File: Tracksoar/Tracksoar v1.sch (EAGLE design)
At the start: 39 parts, among them IC2 74AHC1G125DBV, U1 ATMEGA328P, Y1 16MHZ

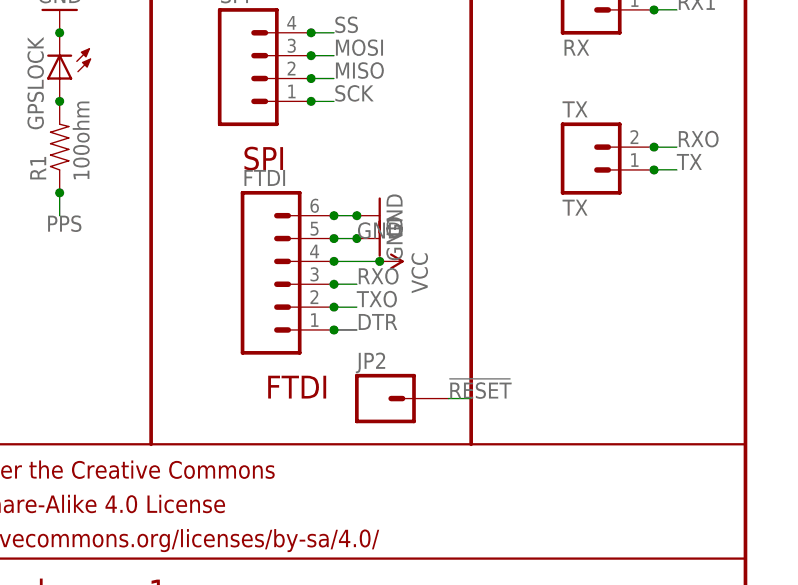
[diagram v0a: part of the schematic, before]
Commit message: replace headers
replaced 2.54mm headers on all production boards with 2mm headers to
resolve daughter board issues.
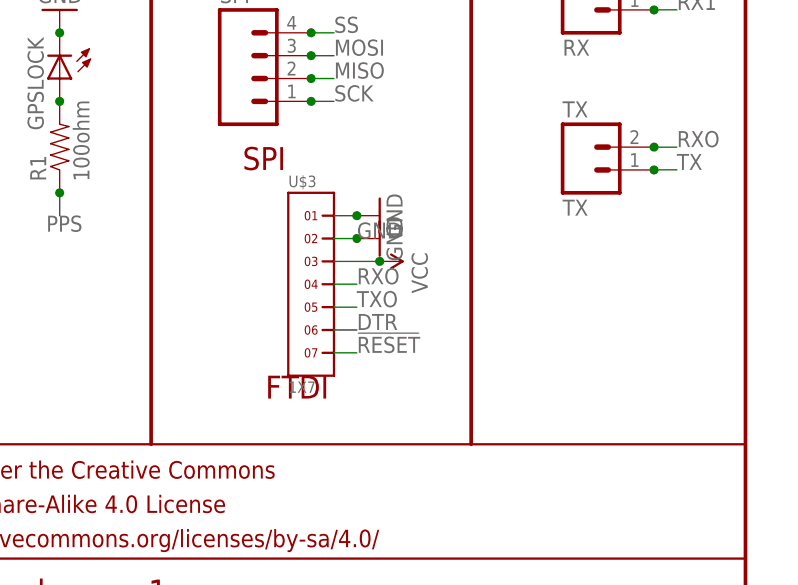
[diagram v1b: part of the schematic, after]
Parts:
- removed FTDI: (no value), SparkFun-Connectors:M06NO_SILK_FEMALE_PTH
- removed JP2: (no value), SparkFun-Connectors:M01PTH
- added U$3: 1X7, headers(2mm):1X7
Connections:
- net !RESET: now also U$3.7; no longer JP2.1
- net DTR: now also U$3.6; no longer FTDI.1
- net GND: now also U$3.1, U$3.2; no longer FTDI.5, FTDI.6
- net RXO: now also U$3.4; no longer FTDI.3
- net TXO: now also U$3.5; no longer FTDI.2
- net VCC: now also U$3.3; no longer FTDI.4
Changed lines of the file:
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@@
 <part name="SUPPLY4" library="SparkFun-Aesthetics" deviceset="VCC" device=""/>
 <part name="SUPPLY5" library="SparkFun-Aesthetics" deviceset="VCC" device=""/>
-<part name="FTDI" library="SparkFun-Connectors" deviceset="M06" device="NO_SILK_FEMALE_PTH"/>
 <part name="SUPPLY7" library="SparkFun-Aesthetics" deviceset="VCC" device=""/>
 <part name="SUPPLY8" library="SparkFun-Aesthetics" deviceset="VCC" device=""/>
@@
 <part name="GPS-ANT" library="SparkFun-RF" deviceset="ANTENNA2" device="SMD3"/>
 <part name="TX1" library="SparkFun-Connectors" deviceset="M02" device="JST-PTH-VERT" value="TX"/>
-<part name="JP2" library="SparkFun-Connectors" deviceset="M01" device="PTH"/>
+<part name="U$3" library="headers(2mm)" deviceset="1X7" device=""/>
 </parts>
 <sheets>
@@
 <instance part="SUPPLY4" gate="G$1" x="55.88" y="160.02" rot="R90"/>
 <instance part="SUPPLY5" gate="G$1" x="55.88" y="152.4" rot="R90"/>
-<instance part="FTDI" gate="G$1" x="198.12" y="53.34"/>
 <instance part="SUPPLY7" gate="G$1" x="25.4" y="60.96" rot="R90"/>
 <instance part="SUPPLY8" gate="G$1" x="25.4" y="58.42" rot="R90"/>
@@
 <instance part="GPS-ANT" gate="G$1" x="165.1" y="165.1" rot="R90"/>
 <instance part="TX1" gate="G$1" x="193.04" y="91.44"/>
-<instance part="JP2" gate="G$1" x="208.28" y="40.64"/>
+<instance part="U$3" gate="G$1" x="200.66" y="53.34"/>
 </instances>
 <busses>
@@
 </segment>
 <segment>
-<pinref part="FTDI" gate="G$1" pin="6"/>
 <wire x1="203.2" y1="60.96" x2="205.74" y2="60.96" width="0.1524" layer="91"/>
 <pinref part="GND22" gate="1" pin="GND"/>
-<junction x="203.2" y="60.96"/>
 <junction x="205.74" y="60.96"/>
+<pinref part="U$3" gate="G$1" pin="1"/>
 </segment>
 <segment>
@@
 </segment>
 <segment>
-<pinref part="FTDI" gate="G$1" pin="5"/>
 <wire x1="203.2" y1="58.42" x2="205.74" y2="58.42" width="0.1524" layer="91"/>
 <label x="205.74" y="58.42" size="1.778" layer="95"/>
-<junction x="203.2" y="58.42"/>
 <pinref part="GND10" gate="1" pin="GND"/>
 <junction x="205.74" y="58.42"/>
+<pinref part="U$3" gate="G$1" pin="2"/>
 </segment>
 <segment>
@@
 </segment>
 <segment>
-<pinref part="FTDI" gate="G$1" pin="4"/>
 <wire x1="203.2" y1="55.88" x2="208.28" y2="55.88" width="0.1524" layer="91"/>
 <pinref part="SUPPLY9" gate="G$1" pin="VCC"/>
-<junction x="203.2" y="55.88"/>
 <junction x="208.28" y="55.88"/>
+<pinref part="U$3" gate="G$1" pin="3"/>
 </segment>
 <segment>
@@
 <net name="DTR" class="0">
 <segment>
-<pinref part="FTDI" gate="G$1" pin="1"/>
 <wire x1="203.2" y1="48.26" x2="205.74" y2="48.26" width="0.1524" layer="91"/>
 <label x="205.74" y="48.26" size="1.778" layer="95"/>
-<junction x="203.2" y="48.26"/>
+<pinref part="U$3" gate="G$1" pin="6"/>
 </segment>
 <segment>
@@
 </segment>
 <segment>
-<pinref part="FTDI" gate="G$1" pin="3"/>
 <wire x1="203.2" y1="53.34" x2="205.74" y2="53.34" width="0.1524" layer="91"/>
 <label x="205.74" y="53.34" size="1.778" layer="95"/>
-<junction x="203.2" y="53.34"/>
+<pinref part="U$3" gate="G$1" pin="4"/>
 </segment>
 </net>
@@
 </segment>
 <segment>
-<pinref part="FTDI" gate="G$1" pin="2"/>
 <wire x1="203.2" y1="50.8" x2="205.74" y2="50.8" width="0.1524" layer="91"/>
 <label x="205.74" y="50.8" size="1.778" layer="95"/>
-<junction x="203.2" y="50.8"/>
+<pinref part="U$3" gate="G$1" pin="5"/>
 </segment>
 </net>
@@
 <net name="!RESET" class="0">
 <segment>
-<pinref part="JP2" gate="G$1" pin="1"/>
-<wire x1="215.9" y1="40.64" x2="218.44" y2="40.64" width="0.1524" layer="91"/>
-<label x="215.9" y="40.64" size="1.778" layer="95"/>
-</segment>
-<segment>
+<wire x1="203.2" y1="45.72" x2="205.74" y2="45.72" width="0.1524" layer="91"/>
+<label x="205.74" y="45.72" size="1.778" layer="95"/>
+<pinref part="U$3" gate="G$1" pin="7"/>
+</segment>
+<segment>

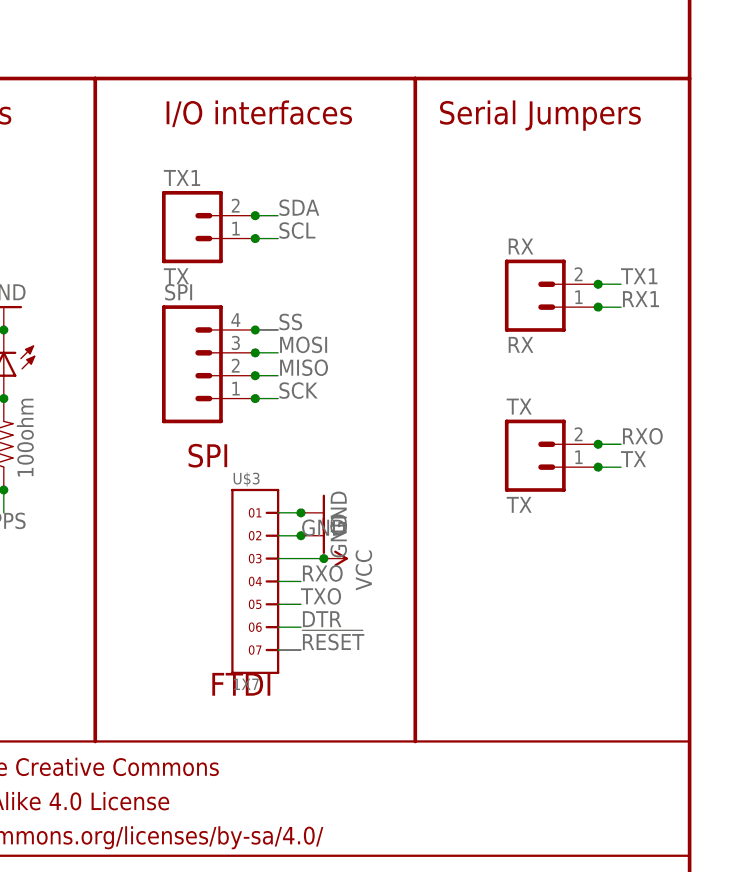
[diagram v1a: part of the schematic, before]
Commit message: Rounded corners
Added rounded corners to the tracksoar v1
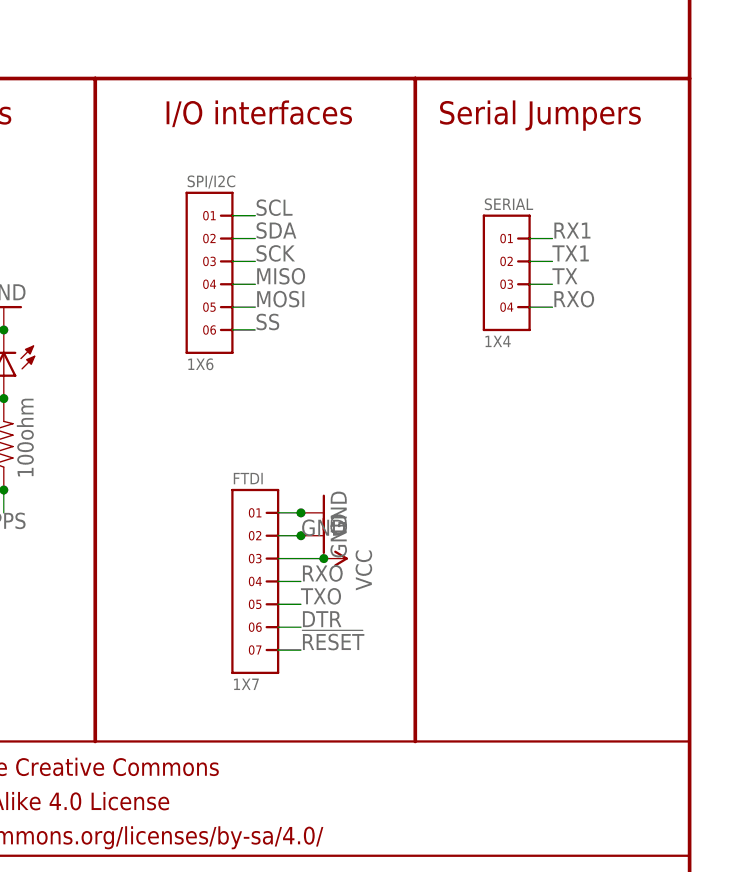
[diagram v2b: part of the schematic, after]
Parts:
- removed RX: RX, SparkFun-Connectors:M02JST-PTH-VERT
- removed SPI: (no value), SparkFun-Connectors:M04JST-PTH-VERT
- removed TX, TX1: TX, SparkFun-Connectors:M02JST-PTH-VERT
- added SERIAL: 1X4, headers(2mm):1X4
- added SPI/I2C: 1X6, headers(2mm):1X6
- renumbered U$3 to FTDI
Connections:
- net MISO: now also SPI/I2C.4; no longer SPI.2
- net MOSI: now also SPI/I2C.5; no longer SPI.3
- net RX1: now also SERIAL.1; no longer RX.1
- net RXO: now also SERIAL.4; no longer TX.2
- net SCK: now also SPI/I2C.3; no longer SPI.1
- net SCL: now also SPI/I2C.1; no longer TX1.1
- net SDA: now also SPI/I2C.2; no longer TX1.2
- net SS: now also SPI/I2C.6; no longer SPI.4
- net TX: now also SERIAL.3; no longer TX.1
- net TX1: now also SERIAL.2; no longer RX.2
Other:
- note removed: "FTDI"
- note removed: "SPI"
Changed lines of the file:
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@@
 <part name="SUPPLY10" library="SparkFun-Aesthetics" deviceset="VCC" device=""/>
 <part name="C5" library="SparkFun-Capacitors" deviceset="CAP" device="0805" value=".1uf"/>
-<part name="TX" library="SparkFun-Connectors" deviceset="M02" device="JST-PTH-VERT" value="TX"/>
-<part name="SPI" library="SparkFun-Connectors" deviceset="M04" device="JST-PTH-VERT"/>
 <part name="FRAME1" library="SparkFun-Aesthetics" deviceset="FRAME-LETTER" device=""/>
 <part name="SUPPLY11" library="SparkFun-Aesthetics" deviceset="VCC" device=""/>
@@
 <part name="GND1" library="SparkFun-Aesthetics" deviceset="GND" device=""/>
 <part name="GND3" library="SparkFun-Aesthetics" deviceset="GND" device=""/>
-<part name="RX" library="SparkFun-Connectors" deviceset="M02" device="JST-PTH-VERT" value="RX"/>
 <part name="GND10" library="SparkFun-Aesthetics" deviceset="GND" device=""/>
 <part name="BMP180" library="SparkFun-Sensors" deviceset="BMP180" device=""/>
@@
 <part name="SHT21" library="sht21" deviceset="SHT21" device=""/>
 <part name="GPS-ANT" library="SparkFun-RF" deviceset="ANTENNA2" device="SMD3"/>
-<part name="TX1" library="SparkFun-Connectors" deviceset="M02" device="JST-PTH-VERT" value="TX"/>
-<part name="U$3" library="headers(2mm)" deviceset="1X7" device=""/>
+<part name="FTDI" library="headers(2mm)" deviceset="1X7" device=""/>
+<part name="SPI/I2C" library="headers(2mm)" deviceset="1X6" device=""/>
+<part name="SERIAL" library="headers(2mm)" deviceset="1X4" device=""/>
 </parts>
 <sheets>
@@
 <text x="190.5" y="104.14" size="2.54" layer="94">I/O interfaces</text>
 <text x="220.98" y="104.14" size="2.54" layer="94">Serial Jumpers</text>
-<text x="193.04" y="66.04" size="2.54" layer="94">SPI</text>
-<text x="195.58" y="40.64" size="2.54" layer="94">FTDI</text>
 <wire x1="147.32" y1="35.56" x2="83.82" y2="35.56" width="0.1524" layer="94"/>
 <text x="111.76" y="104.14" size="1.778" layer="94">Sensors</text>
@@
 <instance part="SUPPLY10" gate="G$1" x="25.4" y="78.74"/>
 <instance part="C5" gate="G$1" x="12.7" y="68.58" rot="R90"/>
-<instance part="TX" gate="G$1" x="231.14" y="66.04"/>
-<instance part="SPI" gate="G$1" x="195.58" y="76.2"/>
 <instance part="FRAME1" gate="G$1" x="0" y="0"/>
 <instance part="FRAME1" gate="G$2" x="147.32" y="0"/>
@@
 <instance part="GND1" gate="1" x="66.04" y="167.64" rot="R90"/>
 <instance part="GND3" gate="1" x="17.78" y="157.48"/>
-<instance part="RX" gate="G$1" x="231.14" y="83.82"/>
 <instance part="GND10" gate="1" x="208.28" y="58.42" rot="R90"/>
 <instance part="BMP180" gate="G$1" x="104.14" y="48.26"/>
@@
 <instance part="SHT21" gate="A" x="121.92" y="83.82"/>
 <instance part="GPS-ANT" gate="G$1" x="165.1" y="165.1" rot="R90"/>
-<instance part="TX1" gate="G$1" x="193.04" y="91.44"/>
-<instance part="U$3" gate="G$1" x="200.66" y="53.34"/>
+<instance part="FTDI" gate="G$1" x="200.66" y="53.34"/>
+<instance part="SPI/I2C" gate="G$1" x="195.58" y="86.36"/>
+<instance part="SERIAL" gate="G$1" x="228.6" y="86.36"/>
 </instances>
 <busses>
@@
 <pinref part="GND22" gate="1" pin="GND"/>
 <junction x="205.74" y="60.96"/>
-<pinref part="U$3" gate="G$1" pin="1"/>
+<pinref part="FTDI" gate="G$1" pin="1"/>
 </segment>
 <segment>
@@
 <pinref part="GND10" gate="1" pin="GND"/>
 <junction x="205.74" y="58.42"/>
-<pinref part="U$3" gate="G$1" pin="2"/>
+<pinref part="FTDI" gate="G$1" pin="2"/>
 </segment>
 <segment>
@@
 <pinref part="SUPPLY9" gate="G$1" pin="VCC"/>
 <junction x="208.28" y="55.88"/>
-<pinref part="U$3" gate="G$1" pin="3"/>
+<pinref part="FTDI" gate="G$1" pin="3"/>
 </segment>
 <segment>
@@
 <wire x1="203.2" y1="48.26" x2="205.74" y2="48.26" width="0.1524" layer="91"/>
 <label x="205.74" y="48.26" size="1.778" layer="95"/>
-<pinref part="U$3" gate="G$1" pin="6"/>
+<pinref part="FTDI" gate="G$1" pin="6"/>
 </segment>
 <segment>
@@
 </segment>
 <segment>
-<pinref part="TX" gate="G$1" pin="2"/>
-<wire x1="238.76" y1="68.58" x2="241.3" y2="68.58" width="0.1524" layer="91"/>
-<label x="241.3" y="68.58" size="1.778" layer="95"/>
-<junction x="238.76" y="68.58"/>
+<wire x1="233.68" y1="83.82" x2="231.14" y2="83.82" width="0.1524" layer="91"/>
+<label x="233.68" y="83.82" size="1.778" layer="95"/>
+<pinref part="SERIAL" gate="G$1" pin="4"/>
 </segment>
 <segment>
 <wire x1="203.2" y1="53.34" x2="205.74" y2="53.34" width="0.1524" layer="91"/>
 <label x="205.74" y="53.34" size="1.778" layer="95"/>
-<pinref part="U$3" gate="G$1" pin="4"/>
+<pinref part="FTDI" gate="G$1" pin="4"/>
 </segment>
 </net>
@@
 <wire x1="203.2" y1="50.8" x2="205.74" y2="50.8" width="0.1524" layer="91"/>
 <label x="205.74" y="50.8" size="1.778" layer="95"/>
-<pinref part="U$3" gate="G$1" pin="5"/>
+<pinref part="FTDI" gate="G$1" pin="5"/>
 </segment>
 </net>
@@
 </segment>
 <segment>
-<pinref part="SPI" gate="G$1" pin="2"/>
-<wire x1="200.66" y1="76.2" x2="203.2" y2="76.2" width="0.1524" layer="91"/>
-<label x="203.2" y="76.2" size="1.778" layer="95"/>
-<junction x="200.66" y="76.2"/>
+<wire x1="200.66" y1="86.36" x2="198.12" y2="86.36" width="0.1524" layer="91"/>
+<label x="200.66" y="86.36" size="1.778" layer="95"/>
+<pinref part="SPI/I2C" gate="G$1" pin="4"/>
 </segment>
 </net>
@@
 </segment>
 <segment>
-<pinref part="SPI" gate="G$1" pin="3"/>
-<wire x1="200.66" y1="78.74" x2="203.2" y2="78.74" width="0.1524" layer="91"/>
-<label x="203.2" y="78.74" size="1.778" layer="95"/>
-<junction x="200.66" y="78.74"/>
+<wire x1="200.66" y1="83.82" x2="198.12" y2="83.82" width="0.1524" layer="91"/>
+<label x="200.66" y="83.82" size="1.778" layer="95"/>
+<pinref part="SPI/I2C" gate="G$1" pin="5"/>
 </segment>
 </net>
@@
 </segment>
 <segment>
-<pinref part="SPI" gate="G$1" pin="1"/>
-<wire x1="200.66" y1="73.66" x2="203.2" y2="73.66" width="0.1524" layer="91"/>
-<label x="203.2" y="73.66" size="1.778" layer="95"/>
-<junction x="200.66" y="73.66"/>
+<wire x1="200.66" y1="88.9" x2="198.12" y2="88.9" width="0.1524" layer="91"/>
+<label x="200.66" y="88.9" size="1.778" layer="95"/>
+<pinref part="SPI/I2C" gate="G$1" pin="3"/>
 </segment>
 </net>
@@
 </segment>
 <segment>
-<pinref part="SPI" gate="G$1" pin="4"/>
-<wire x1="200.66" y1="81.28" x2="203.2" y2="81.28" width="0.1524" layer="91"/>
-<label x="203.2" y="81.28" size="1.778" layer="95"/>
-<junction x="200.66" y="81.28"/>
+<wire x1="200.66" y1="81.28" x2="198.12" y2="81.28" width="0.1524" layer="91"/>
+<label x="200.66" y="81.28" size="1.778" layer="95"/>
+<pinref part="SPI/I2C" gate="G$1" pin="6"/>
 </segment>
 </net>
@@
 </segment>
 <segment>
-<pinref part="RX" gate="G$1" pin="2"/>
-<wire x1="238.76" y1="86.36" x2="241.3" y2="86.36" width="0.1524" layer="91"/>
-<label x="241.3" y="86.36" size="1.778" layer="95"/>
-<junction x="238.76" y="86.36"/>
+<label x="233.68" y="88.9" size="1.778" layer="95"/>
+<pinref part="SERIAL" gate="G$1" pin="2"/>
+<wire x1="231.14" y1="88.9" x2="233.68" y2="88.9" width="0.1524" layer="91"/>
 </segment>
 </net>
@@
 </segment>
 <segment>
-<pinref part="TX1" gate="G$1" pin="2"/>
-<wire x1="200.66" y1="93.98" x2="203.2" y2="93.98" width="0.1524" layer="91"/>
-<label x="203.2" y="93.98" size="1.778" layer="95"/>
-<junction x="200.66" y="93.98"/>
+<wire x1="200.66" y1="91.44" x2="198.12" y2="91.44" width="0.1524" layer="91"/>
+<label x="200.66" y="91.44" size="1.778" layer="95"/>
+<pinref part="SPI/I2C" gate="G$1" pin="2"/>
 </segment>
 </net>
@@
 </segment>
 <segment>
-<pinref part="TX1" gate="G$1" pin="1"/>
-<wire x1="200.66" y1="91.44" x2="203.2" y2="91.44" width="0.1524" layer="91"/>
-<label x="203.2" y="91.44" size="1.778" layer="95"/>
-<junction x="200.66" y="91.44"/>
+<wire x1="200.66" y1="93.98" x2="198.12" y2="93.98" width="0.1524" layer="91"/>
+<label x="200.66" y="93.98" size="1.778" layer="95"/>
+<pinref part="SPI/I2C" gate="G$1" pin="1"/>
 </segment>
 </net>
@@
 </segment>
 <segment>
-<pinref part="RX" gate="G$1" pin="1"/>
-<wire x1="238.76" y1="83.82" x2="241.3" y2="83.82" width="0.1524" layer="91"/>
-<label x="241.3" y="83.82" size="1.778" layer="95"/>
-<junction x="238.76" y="83.82"/>
+<label x="233.68" y="91.44" size="1.778" layer="95"/>
+<pinref part="SERIAL" gate="G$1" pin="1"/>
+<wire x1="231.14" y1="91.44" x2="233.68" y2="91.44" width="0.1524" layer="91"/>
 </segment>
 </net>
@@
 </segment>
 <segment>
-<pinref part="TX" gate="G$1" pin="1"/>
-<wire x1="238.76" y1="66.04" x2="241.3" y2="66.04" width="0.1524" layer="91"/>
-<label x="241.3" y="66.04" size="1.778" layer="95"/>
-<junction x="238.76" y="66.04"/>
+<wire x1="233.68" y1="86.36" x2="231.14" y2="86.36" width="0.1524" layer="91"/>
+<label x="233.68" y="86.36" size="1.778" layer="95"/>
+<pinref part="SERIAL" gate="G$1" pin="3"/>
 </segment>
 </net>
@@
 <wire x1="203.2" y1="45.72" x2="205.74" y2="45.72" width="0.1524" layer="91"/>
 <label x="205.74" y="45.72" size="1.778" layer="95"/>
-<pinref part="U$3" gate="G$1" pin="7"/>
-</segment>
-<segment>
+<pinref part="FTDI" gate="G$1" pin="7"/>
+</segment>
+<segment>

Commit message: fixed silk screen
fixed minor errors and overlaps on the silkscreen
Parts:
- removed JP1: M02JST-PTH-VERT, SparkFun-Connectors:M02JST-PTH-VERT
- added U$3: 1X2, headers(2mm):1X2
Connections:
- net 15V: now also U$3.2; no longer JP1.2
- net GND: now also U$3.1; no longer JP1.1
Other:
- moved on the sheet: C7, C8, C9, D1, L2, R10, R8, R9
